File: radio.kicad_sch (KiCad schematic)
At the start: 41 parts, among them U11 MAX5865

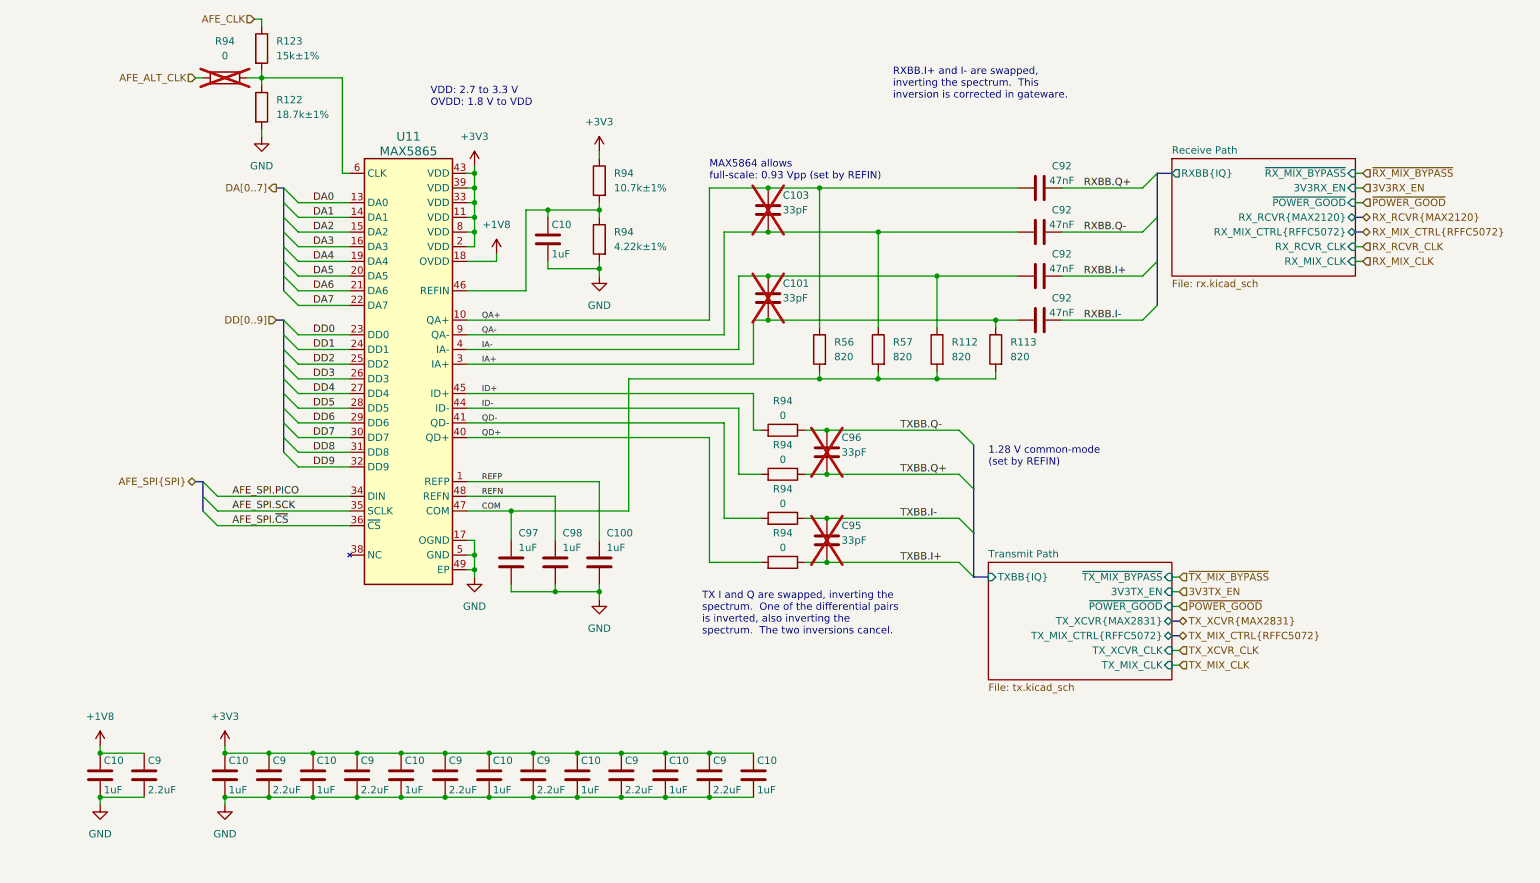
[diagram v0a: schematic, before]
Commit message: add regulator for analog 3.3 V supply
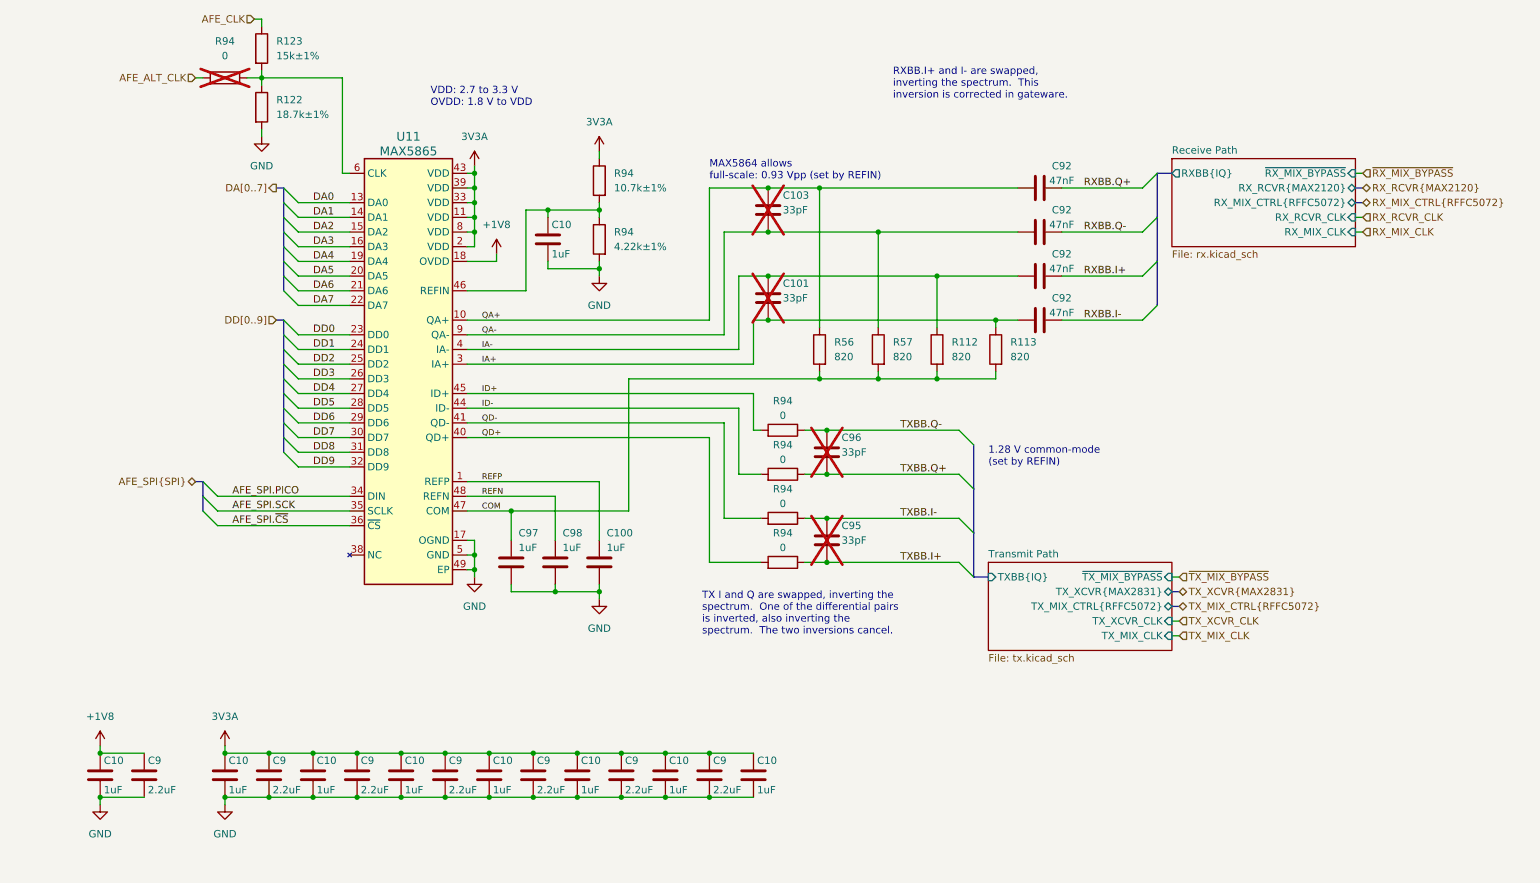
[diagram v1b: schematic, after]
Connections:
- net +3V3 renamed 3V3A
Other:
- sheet Receive Path ports: added none; removed 3V3RX_EN, ~{POWER_GOOD}
- sheet Transmit Path ports: added none; removed 3V3TX_EN, ~{POWER_GOOD}

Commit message: add analog baseband common-mode chokes
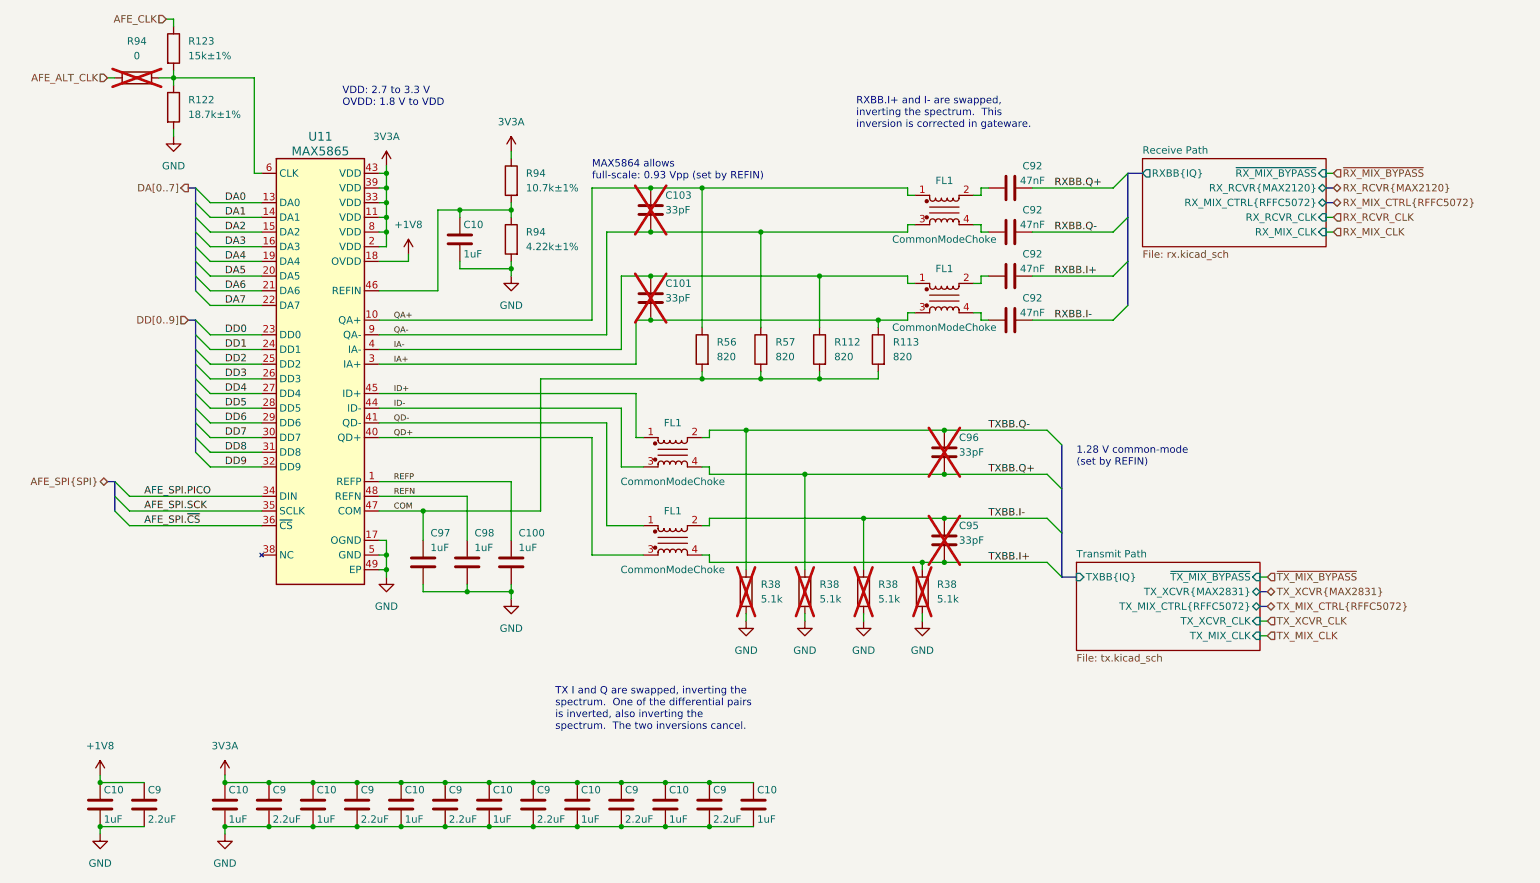
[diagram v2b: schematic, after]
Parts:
- removed R94 (x4): 0, Resistor_SMD:R_0201_0603Metric, symbol Device:R
- added FL1 (x4): CommonModeChoke, mainboard:L_CommonModeChoke_Murata_DLM0NS, symbol Device:Filter_EMI_CommonMode
- added R38 (x4): 5.1k, Resistor_SMD:R_0402_1005Metric, symbol Device:R
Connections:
- net GND: now also R38.2, R38.2, R38.2, R38.2
- net IA+: now also FL1.3; no longer C92.1
- net IA-: now also FL1.1; no longer C92.1
- net ID+: now also FL1.1
- net ID-: now also FL1.3
- net QA+: now also FL1.1; no longer C92.1
- net QA-: now also FL1.3; no longer C92.1
- net QD+: now also FL1.3
- net QD-: now also FL1.1
- net TXBB.I+: now also FL1.4, R38.1
- net TXBB.I-: now also FL1.2, R38.1
- net TXBB.Q+: now also FL1.4, R38.1
- net TXBB.Q-: now also FL1.2, R38.1
- new net: C92.1, FL1.2 (x2)
- new net: C92.1, FL1.4 (x2)
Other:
- moved on the sheet: C10, C100, C101, C103, C9, C92, C95, C96, C97, C98, R112, R113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

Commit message: Add footprints
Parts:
- R112, R113, R56, R57: footprint (none) -> Resistor_SMD:R_0201_0603Metric
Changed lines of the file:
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@@
       (effects (font (size 1.27 1.27)) (justify right))
     )
-    (property "Footprint" "" (at 170.688 95.25 90)
+    (property "Footprint" "Resistor_SMD:R_0201_0603Metric" (at 170.688 95.25 90)
       (effects (font (size 1.27 1.27)) hide)
     )
@@
       (effects (font (size 1.27 1.27)) (justify right))
     )
-    (property "Footprint" "" (at 160.528 95.25 90)
+    (property "Footprint" "Resistor_SMD:R_0201_0603Metric" (at 160.528 95.25 90)
       (effects (font (size 1.27 1.27)) hide)
     )
@@
       (effects (font (size 1.27 1.27)) (justify right))
     )
-    (property "Footprint" "" (at 150.368 95.25 90)
+    (property "Footprint" "Resistor_SMD:R_0201_0603Metric" (at 150.368 95.25 90)
       (effects (font (size 1.27 1.27)) hide)
     )
@@
       (effects (font (size 1.27 1.27)) (justify right))
     )
-    (property "Footprint" "" (at 140.208 95.25 90)
-      (effects (font (size 1.27 1.27)) hide)
-    )
+    (property "Footprint" "Resistor_SMD:R_0201_0603Metric" (at 140.208 95.25 90)
+      (effects (font (size 1.27 1.27)) hide)
+    )

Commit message: layout wip
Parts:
- removed C10: 1uF, Capacitor_SMD:C_0201_0603Metric, symbol Device:C
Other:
- note added: "MAX5865 allows full-scale: 0.93 Vpp (set by REFIN)"
- note removed: "MAX5864 allows full-scale: 0.93 Vpp (set by REFIN)"
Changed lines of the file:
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@@
   (junction (at 101.6 177.8) (diameter 0) (color 0 0 0 0)
   )
-  (junction (at 63.5 177.8) (diameter 0) (color 0 0 0 0)
-  )
   (junction (at 166.37 124.46) (diameter 0) (color 0 0 0 0)
   )
@@
   (junction (at 124.46 170.18) (diameter 0) (color 0 0 0 0)
   )
-  (junction (at 55.88 177.8) (diameter 0) (color 0 0 0 0)
-  )
   (junction (at 93.98 170.18) (diameter 0) (color 0 0 0 0)
   )
   (junction (at 158.75 82.55) (diameter 0) (color 0 0 0 0)
   )
+  (junction (at 63.5 170.18) (diameter 0) (color 0 0 0 0)
+  )
   (junction (at 138.43 67.31) (diameter 0) (color 0 0 0 0)
   )
@@
   (junction (at 116.84 170.18) (diameter 0) (color 0 0 0 0)
   )
+  (junction (at 63.5 177.8) (diameter 0) (color 0 0 0 0)
+  )
   (junction (at 132.08 170.18) (diameter 0) (color 0 0 0 0)
   )
@@
   (junction (at 180.34 116.84) (diameter 0) (color 0 0 0 0)
   )
-  (junction (at 55.88 170.18) (diameter 0) (color 0 0 0 0)
-  )
   (junction (at 34.29 177.8) (diameter 0) (color 0 0 0 0)
   )
@@
   (junction (at 168.91 90.17) (diameter 0) (color 0 0 0 0)
   )
-  (junction (at 63.5 170.18) (diameter 0) (color 0 0 0 0)
-  )
   (junction (at 158.75 100.33) (diameter 0) (color 0 0 0 0)
   )
@@
     (stroke (width 0) (type default))
   )
-  (wire (pts (xy 55.88 170.18) (xy 55.88 168.91))
-    (stroke (width 0) (type default))
-  )
   (wire (pts (xy 82.55 107.95) (xy 121.92 107.95))
     (stroke (width 0) (type default))
@@
     (stroke (width 0) (type default))
   )
-  (wire (pts (xy 55.88 177.8) (xy 55.88 179.07))
-    (stroke (width 0) (type default))
-  )
   (wire (pts (xy 175.26 83.82) (xy 173.99 83.82))
     (stroke (width 0) (type default))
@@
     (stroke (width 0) (type default))
   )
-  (wire (pts (xy 55.88 170.18) (xy 63.5 170.18))
-    (stroke (width 0) (type default))
-  )
   (wire (pts (xy 53.34 113.03) (xy 62.23 113.03))
     (stroke (width 0) (type default))
@@
     (stroke (width 0) (type default))
   )
+  (wire (pts (xy 63.5 177.8) (xy 63.5 179.07))
+    (stroke (width 0) (type default))
+  )
   (wire (pts (xy 127 97.79) (xy 127 90.17))
     (stroke (width 0) (type default))
@@
     (stroke (width 0) (type default))
   )
+  (wire (pts (xy 63.5 168.91) (xy 63.5 170.18))
+    (stroke (width 0) (type default))
+  )
   (wire (pts (xy 129.54 82.55) (xy 158.75 82.55))
     (stroke (width 0) (type default))
@@
     (stroke (width 0) (type default))
   )
-  (wire (pts (xy 55.88 177.8) (xy 63.5 177.8))
-    (stroke (width 0) (type default))
-  )
   (wire (pts (xy 110.49 123.19) (xy 110.49 100.33))
     (stroke (width 0) (type default))
@@
     (stroke (width 0) (type default))
   )
-  (text "MAX5864 allows\nfull-scale: 0.93 Vpp (set by REFIN)"
+  (text "MAX5865 allows\nfull-scale: 0.93 Vpp (set by REFIN)"
     (at 119.38 66.04 0)
     (effects (font (size 1.27 1.27)) (justify left bottom))
@@
       (effects (font (size 1.524 1.524)) hide)
     )
-    (property "Datasheet" "" (at 90.17 132.08 0)
+    (property "Datasheet" "~" (at 90.17 132.08 0)
       (effects (font (size 1.524 1.524)) hide)
     )
@@
       (effects (font (size 1.524 1.524)) hide)
     )
-    (property "Datasheet" "" (at 180.34 113.03 0)
+    (property "Datasheet" "~" (at 180.34 113.03 0)
       (effects (font (size 1.524 1.524)) hide)
     )
@@
       (effects (font (size 1.524 1.524)) hide)
     )
-    (property "Datasheet" "" (at 129.54 86.36 0)
+    (property "Datasheet" "~" (at 129.54 86.36 0)
       (effects (font (size 1.524 1.524)) hide)
     )
@@
       (effects (font (size 1.524 1.524)) hide)
     )
-    (property "Datasheet" "" (at 129.54 71.12 0)
+    (property "Datasheet" "~" (at 129.54 71.12 0)
       (effects (font (size 1.524 1.524)) hide)
     )
@@
       (effects (font (size 1.524 1.524)) hide)
     )
-    (property "Datasheet" "" (at 105.41 132.08 0)
+    (property "Datasheet" "~" (at 105.41 132.08 0)
       (effects (font (size 1.524 1.524)) hide)
     )
@@
     )
   )
-  (symbol (lib_name "GND_1") (lib_id "power:GND") (at 55.88 179.07 0) (unit 1)
+  (symbol (lib_name "GND_1") (lib_id "power:GND") (at 63.5 179.07 0) (unit 1)
     (in_bom yes) (on_board yes) (dnp no) (fields_autoplaced)
-    (property "Reference" "#PWR0186" (at 55.88 185.42 0)
+    (property "Reference" "#PWR0186" (at 63.5 185.42 0)
       (effects (font (size 1.27 1.27)) hide)
     )
-    (property "Value" "GND" (at 55.88 184.15 0)
+    (property "Value" "GND" (at 63.5 184.15 0)
       (effects (font (size 1.27 1.27)))
     )
-    (property "Footprint" "" (at 55.88 179.07 0)
+    (property "Footprint" "" (at 63.5 179.07 0)
       (effects (font (size 1.27 1.27)) hide)
     )
-    (property "Datasheet" "" (at 55.88 179.07 0)
+    (property "Datasheet" "" (at 63.5 179.07 0)
       (effects (font (size 1.27 1.27)) hide)
     )
@@
       (effects (font (size 1.524 1.524)) hide)
     )
-    (property "Datasheet" "" (at 180.34 128.27 0)
+    (property "Datasheet" "~" (at 180.34 128.27 0)
       (effects (font (size 1.524 1.524)) hide)
     )
@@
     )
   )
-  (symbol (lib_id "Device:C") (at 55.88 173.99 0) (unit 1)
-    (in_bom yes) (on_board yes) (dnp no)
-    (property "Reference" "C10" (at 56.515 171.45 0)
-      (effects (font (size 1.27 1.27)) (justify left))
-    )
-    (property "Value" "1uF" (at 56.515 176.53 0)
-      (effects (font (size 1.27 1.27)) (justify left))
-    )
-    (property "Footprint" "Capacitor_SMD:C_0201_0603Metric" (at 56.8452 177.8 0)
-      (effects (font (size 1.27 1.27)) hide)
-    )
-    (property "Datasheet" "~" (at 55.88 173.99 0)
-      (effects (font (size 1.27 1.27)) hide)
-    )
-    (property "Part Number" "GRM033R61A105ME44D" (at 55.88 173.99 0)
-      (effects (font (size 1.27 1.27)) hide)
-    )
-    (property "Substitution" "GRM033R61A105ME44*, GRM033R61C105ME15*, Samsung CL03A105MO3NRN*" (at 55.88 173.99 0)
-      (effects (font (size 1.27 1.27)) hide)
-    )
-    (property "Description" "CAP CER 1UF 10V X5R 0201" (at 55.88 173.99 0)
-      (effects (font (size 1.27 1.27)) hide)
-    )
-    (property "Manufacturer" "Murata" (at 55.88 173.99 0)
-      (effects (font (size 1.27 1.27)) hide)
-    )
-    (pin "1")
-    (pin "2")
-    (instances
-      (project "mainboard"
-        (path "/fb621148-8145-4217-9712-738e1b5a4823/00000000-0000-0000-0000-00005da7baf4"
-          (reference "C10") (unit 1)
-        )
-        (path "/fb621148-8145-4217-9712-738e1b5a4823/4ec621be-184d-4855-a96d-f6fa2a788a77"
-          (reference "C63") (unit 1)
-        )
-      )
-    )
-  )
   (symbol (lib_id "Device:R") (at 146.05 137.16 0) (unit 1)
     (in_bom yes) (on_board yes) (dnp yes) (fields_autoplaced)
@@
     )
   )
-  (symbol (lib_id "support_hardware:3V3A") (at 55.88 168.91 0) (unit 1)
+  (symbol (lib_id "support_hardware:3V3A") (at 63.5 168.91 0) (unit 1)
     (in_bom yes) (on_board yes) (dnp no) (fields_autoplaced)
-    (property "Reference" "#PWR0302" (at 55.88 172.72 0)
+    (property "Reference" "#PWR0302" (at 63.5 172.72 0)
       (effects (font (size 1.27 1.27)) hide)
     )
-    (property "Value" "3V3A" (at 55.88 163.83 0)
+    (property "Value" "3V3A" (at 63.5 163.83 0)
       (effects (font (size 1.27 1.27)))
     )
-    (property "Footprint" "" (at 55.88 168.91 0)
+    (property "Footprint" "" (at 63.5 168.91 0)
       (effects (font (size 1.27 1.27)) hide)
     )
-    (property "Datasheet" "" (at 55.88 168.91 0)
+    (property "Datasheet" "" (at 63.5 168.91 0)
       (effects (font (size 1.27 1.27)) hide)
     )
@@
       (effects (font (size 1.524 1.524)) hide)
     )
-    (property "Datasheet" "" (at 97.79 132.08 0)
+    (property "Datasheet" "~" (at 97.79 132.08 0)
       (effects (font (size 1.524 1.524)) hide)
     )
